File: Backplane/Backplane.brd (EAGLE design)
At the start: 184.2 x 99.1 mm, 32 parts, among them X1 FAC64S, X2 FAC64S, X3 FAC64S, X4 FAC64S, X5 FAC64S, X6 FAC64S, X7 FAC64S, X9 5566-20

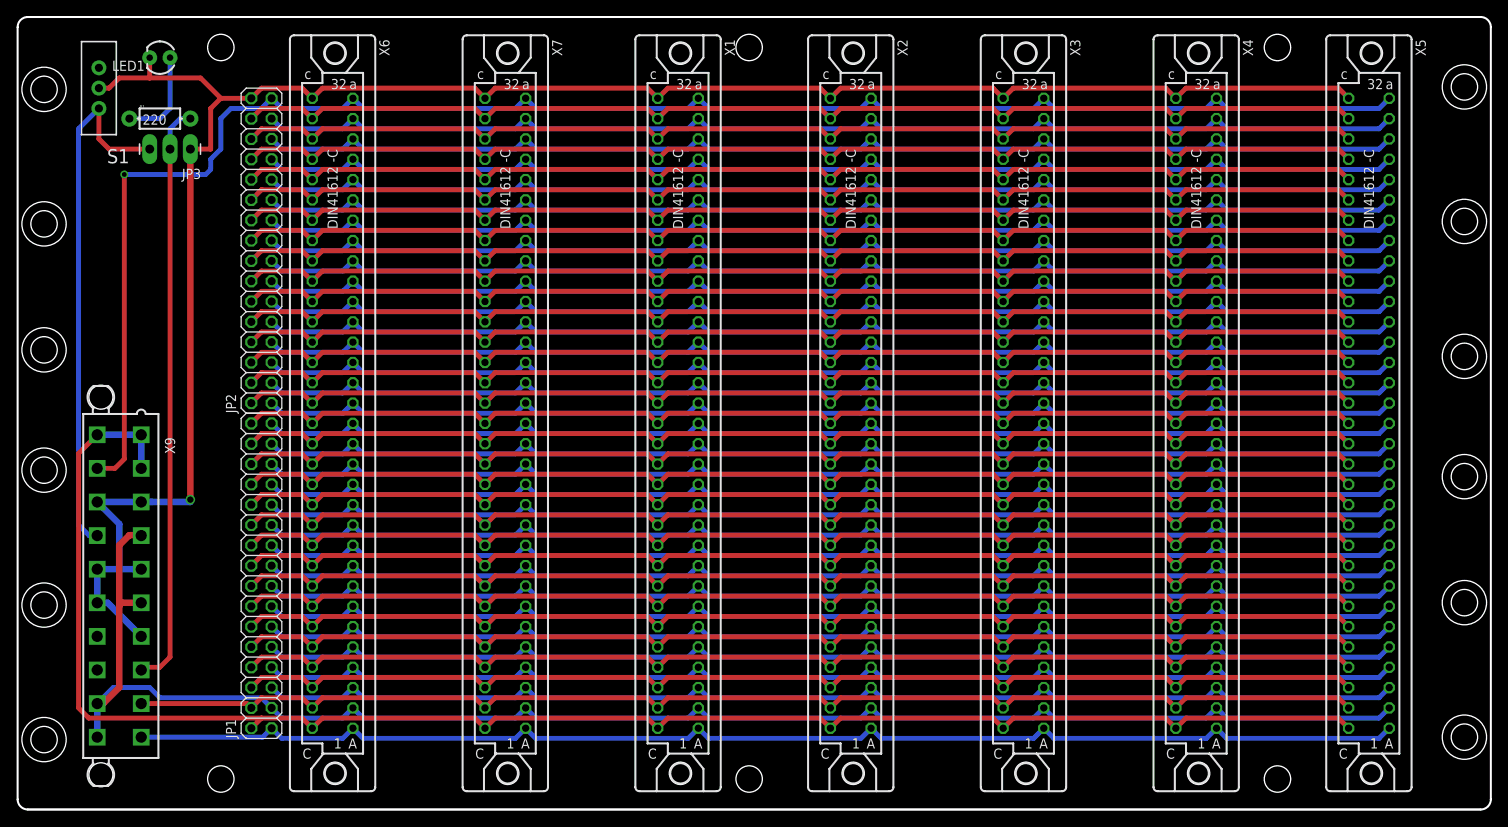
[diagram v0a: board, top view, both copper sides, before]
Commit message: Fixed fit between backplane & enclosure
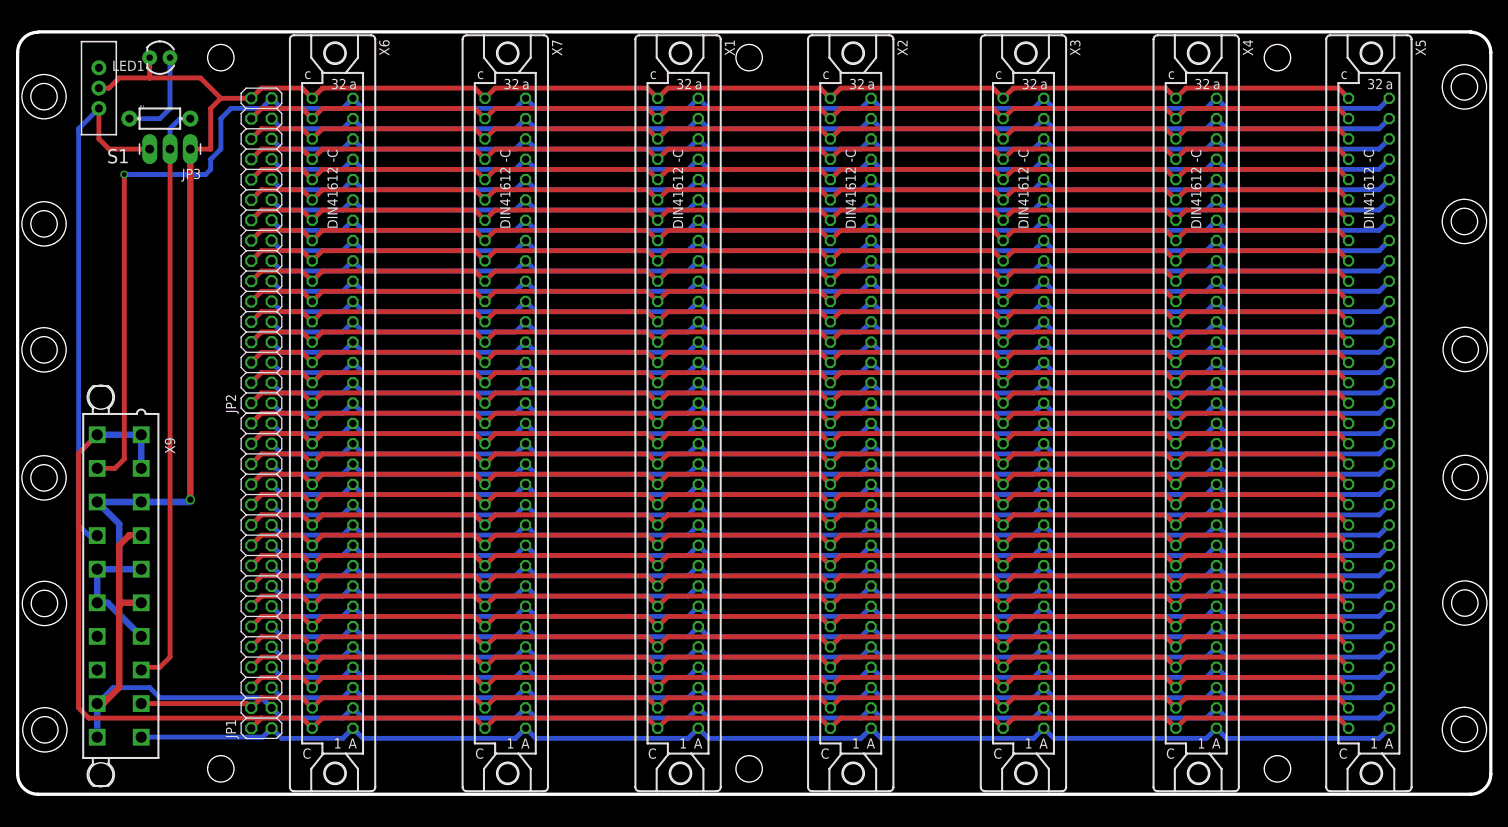
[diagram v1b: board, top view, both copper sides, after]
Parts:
- removed U$11, U$12, U$15, U$16: (no value), SparkFun-Electromechanical:STAND-OFF
- added U$3, U$4, U$5, U$6: (no value), SparkFun-Electromechanical:STAND-OFF
- R1: value 220 -> (none)
- moved U$1 1.27 mm to (95.2, 6.35)
- moved U$7 1.27 mm to (161.3, 6.35)
- moved U$9 1.27 mm to (29.2, 6.35)
- moved U$10 1.27 mm to (29.2, 95.2)
- moved U$2 1.27 mm to (95.2, 95.2)
- moved U$8 1.27 mm to (161.3, 95.2)
- moved U$22 1.22 mm to (7.21, 11.2)
- moved U$19 0.97 mm to (7.11, 42.7)
- moved U$24 0.91 mm to (7.11, 90.4)
- moved U$21 0.21 mm to (7.16, 27.0), turned to 90 degrees
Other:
- board size 184.2 x 99.1 mm -> 184.2 x 95.3 mm
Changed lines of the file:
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@@
 <board>
 <plain>
-<wire x1="186.69" y1="100.33" x2="5.08" y2="100.33" width="0.254" layer="46"/>
-<wire x1="5.08" y1="100.33" x2="3.81" y2="99.06" width="0.254" layer="46" curve="90"/>
-<wire x1="3.81" y1="99.06" x2="3.81" y2="2.54" width="0.254" layer="46"/>
-<wire x1="3.81" y1="2.54" x2="5.08" y2="1.27" width="0.254" layer="46" curve="90"/>
-<wire x1="186.69" y1="1.27" x2="187.96" y2="2.54" width="0.254" layer="46" curve="90"/>
-<wire x1="187.96" y1="2.54" x2="187.96" y2="99.06" width="0.254" layer="46"/>
-<wire x1="187.96" y1="99.06" x2="186.69" y2="100.33" width="0.254" layer="46" curve="90"/>
-<hole x="184.658" y="10.3124" drill="5.5372"/>
-<hole x="184.658" y="27.1272" drill="5.5372"/>
-<hole x="184.658" y="42.8752" drill="5.5372"/>
-<hole x="184.658" y="57.912" drill="5.5372"/>
 <hole x="184.658" y="74.7776" drill="5.5372"/>
 <hole x="184.658" y="91.5924" drill="5.5372"/>
-<hole x="7.112" y="91.2876" drill="5.5372"/>
+<hole x="7.112" y="90.3732" drill="5.5372"/>
 <hole x="7.112" y="74.4728" drill="5.5372"/>
 <hole x="7.112" y="58.7248" drill="5.5372"/>
-<hole x="7.112" y="43.688" drill="5.5372"/>
-<hole x="7.112" y="26.8224" drill="5.5372"/>
-<hole x="7.112" y="10.0076" drill="5.5372"/>
-<text x="137.16" y="54.61" size="1.778" layer="22" rot="MR270">Straight conn DIN41612-C AMP 535059-4</text>
-<text x="123.19" y="54.61" size="1.778" layer="22" rot="MR270">RA conn DIN41612-C AMP 650945-5</text>
+<hole x="7.112" y="42.7228" drill="5.5372"/>
+<hole x="7.1628" y="27.0256" drill="5.5372"/>
+<hole x="7.2136" y="11.2268" drill="5.5372"/>
+<text x="137.16" y="90.17" size="1.778" layer="22" rot="MR270">Straight conn DIN41612-C AMP 535059-4</text>
+<text x="123.19" y="90.17" size="1.778" layer="22" rot="MR270">RA conn DIN41612-C AMP 650945-5</text>
 <text x="31.2928" y="75.6412" size="1.778" layer="22" rot="MR270">64 Pin Terminal Samtek TLW-132-06-F-D SLW-132-01-F-D</text>
-<wire x1="186.69" y1="1.27" x2="5.08" y2="1.27" width="0.3048" layer="46"/>
+<wire x1="185.42" y1="3.175" x2="6.35" y2="3.175" width="0.4064" layer="46"/>
+<wire x1="6.35" y1="3.175" x2="3.81" y2="5.715" width="0.4064" layer="46" curve="-90"/>
+<wire x1="3.81" y1="5.715" x2="3.81" y2="95.885" width="0.4064" layer="46"/>
+<wire x1="3.81" y1="95.885" x2="6.35" y2="98.425" width="0.4064" layer="46" curve="-90"/>
+<wire x1="185.42" y1="98.425" x2="187.96" y2="95.885" width="0.4064" layer="46" curve="-90"/>
+<wire x1="187.96" y1="95.885" x2="187.96" y2="5.715" width="0.4064" layer="46"/>
+<wire x1="187.96" y1="5.715" x2="185.42" y2="3.175" width="0.4064" layer="46" curve="-90"/>
+<hole x="184.7596" y="58.7756" drill="5.5372"/>
+<hole x="184.7596" y="42.7736" drill="5.5372"/>
+<hole x="184.7088" y="27.0764" drill="5.5372"/>
+<hole x="184.658" y="11.2776" drill="5.5372"/>
+<wire x1="185.5216" y1="98.4758" x2="6.4516" y2="98.4758" width="0.4064" layer="46"/>
 </plain>
 <attributes>
@@
 <element name="X6" library="con-vg" package="FAC64S" value="FAC64S" x="43.18" y="50.8" rot="R180"/>
 <element name="X7" library="con-vg" package="FAC64S" value="FAC64S" x="64.77" y="50.8" rot="R180"/>
-<element name="U$1" library="SparkFun-Electromechanical" package="STAND-OFF" value="" x="95.25" y="5.08" rot="R180"/>
-<element name="U$2" library="SparkFun-Electromechanical" package="STAND-OFF" value="" x="95.25" y="96.52" rot="R180"/>
-<element name="U$7" library="SparkFun-Electromechanical" package="STAND-OFF" value="" x="161.29" y="5.08" rot="R180"/>
-<element name="U$8" library="SparkFun-Electromechanical" package="STAND-OFF" value="" x="161.29" y="96.52" rot="R180"/>
-<element name="U$9" library="SparkFun-Electromechanical" package="STAND-OFF" value="" x="29.21" y="5.08" rot="R180"/>
-<element name="U$10" library="SparkFun-Electromechanical" package="STAND-OFF" value="" x="29.21" y="96.52" rot="R180"/>
-<element name="U$11" library="SparkFun-Electromechanical" package="STAND-OFF" value="" x="184.658" y="57.912" rot="R180"/>
-<element name="U$12" library="SparkFun-Electromechanical" package="STAND-OFF" value="" x="184.658" y="42.8752" rot="R180"/>
+<element name="U$1" library="SparkFun-Electromechanical" package="STAND-OFF" value="" x="95.25" y="6.35" rot="R180"/>
+<element name="U$2" library="SparkFun-Electromechanical" package="STAND-OFF" value="" x="95.25" y="95.25" rot="R180"/>
+<element name="U$7" library="SparkFun-Electromechanical" package="STAND-OFF" value="" x="161.29" y="6.35" rot="R180"/>
+<element name="U$8" library="SparkFun-Electromechanical" package="STAND-OFF" value="" x="161.29" y="95.25" rot="R180"/>
+<element name="U$9" library="SparkFun-Electromechanical" package="STAND-OFF" value="" x="29.21" y="6.35" rot="R180"/>
+<element name="U$10" library="SparkFun-Electromechanical" package="STAND-OFF" value="" x="29.21" y="95.25" rot="R180"/>
 <element name="U$13" library="SparkFun-Electromechanical" package="STAND-OFF" value="" x="184.658" y="74.7776" rot="R180"/>
 <element name="U$14" library="SparkFun-Electromechanical" package="STAND-OFF" value="" x="184.658" y="91.5924" rot="R180"/>
-<element name="U$15" library="SparkFun-Electromechanical" package="STAND-OFF" value="" x="184.658" y="27.1272"/>
-<element name="U$16" library="SparkFun-Electromechanical" package="STAND-OFF" value="" x="184.658" y="10.3124"/>
-<element name="U$19" library="SparkFun-Electromechanical" package="STAND-OFF" value="" x="7.112" y="43.688"/>
+<element name="U$19" library="SparkFun-Electromechanical" package="STAND-OFF" value="" x="7.112" y="42.7228"/>
 <element name="U$20" library="SparkFun-Electromechanical" package="STAND-OFF" value="" x="7.112" y="58.7248"/>
-<element name="U$21" library="SparkFun-Electromechanical" package="STAND-OFF" value="" x="7.112" y="26.8224"/>
-<element name="U$22" library="SparkFun-Electromechanical" package="STAND-OFF" value="" x="7.112" y="10.0076"/>
+<element name="U$21" library="SparkFun-Electromechanical" package="STAND-OFF" value="" x="7.1628" y="27.0256" rot="R90"/>
+<element name="U$22" library="SparkFun-Electromechanical" package="STAND-OFF" value="" x="7.2136" y="11.2268"/>
 <element name="U$23" library="SparkFun-Electromechanical" package="STAND-OFF" value="" x="7.112" y="74.4728" rot="R180"/>
-<element name="U$24" library="SparkFun-Electromechanical" package="STAND-OFF" value="" x="7.112" y="91.2876" rot="R180"/>
+<element name="U$24" library="SparkFun-Electromechanical" package="STAND-OFF" value="" x="7.112" y="90.3732" rot="R180"/>
 <element name="JP1" library="pinhead" package="2X16" value="" x="34.29" y="30.48" rot="R90"/>
 <element name="JP2" library="pinhead" package="2X16" value="" x="34.29" y="71.12" rot="R90"/>
 <element name="S1" library="SparkFun-Electromechanical" package="SWITCH-SPDT" value="" x="13.97" y="91.44" rot="R180"/>
 <element name="LED1" library="SparkFun-LED" package="LED3MM" value="" x="21.59" y="95.25" rot="R180"/>
-<element name="R1" library="SparkFun-Passives" package="AXIAL-0.3-KIT" value="220" x="21.59" y="87.63"/>
+<element name="R1" library="SparkFun-Passives" package="AXIAL-0.3-KIT" value="" x="21.59" y="87.63"/>
 <element name="JP3" library="SparkFun-Connectors" package="1X03_LONGPADS" value="" x="25.4" y="83.82" rot="R180"/>
 <element name="X9" library="con-molex" package="5566-20" value="5566-20" x="16.51" y="29.21" rot="R90">
@@
 <attribute name="OC_FARNELL" value="unknown" x="16.51" y="29.21" size="1.778" layer="27" rot="R90" display="off"/>
 </element>
+<element name="U$3" library="SparkFun-Electromechanical" package="STAND-OFF" value="" x="184.7596" y="42.7736" rot="MR0"/>
+<element name="U$4" library="SparkFun-Electromechanical" package="STAND-OFF" value="" x="184.7596" y="58.7756" rot="MR0"/>
+<element name="U$5" library="SparkFun-Electromechanical" package="STAND-OFF" value="" x="184.7088" y="27.0764" rot="MR90"/>
+<element name="U$6" library="SparkFun-Electromechanical" package="STAND-OFF" value="" x="184.658" y="11.2776" rot="MR0"/>
 </elements>
 <signals>
